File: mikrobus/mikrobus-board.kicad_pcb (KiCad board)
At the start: 2 copper layers, 66 x 63.5 mm, 9 parts, among them J1 Conn_01x06, P3 microBus_1, P4 microBus_2, P5 microBus_1, P6 microBus_2

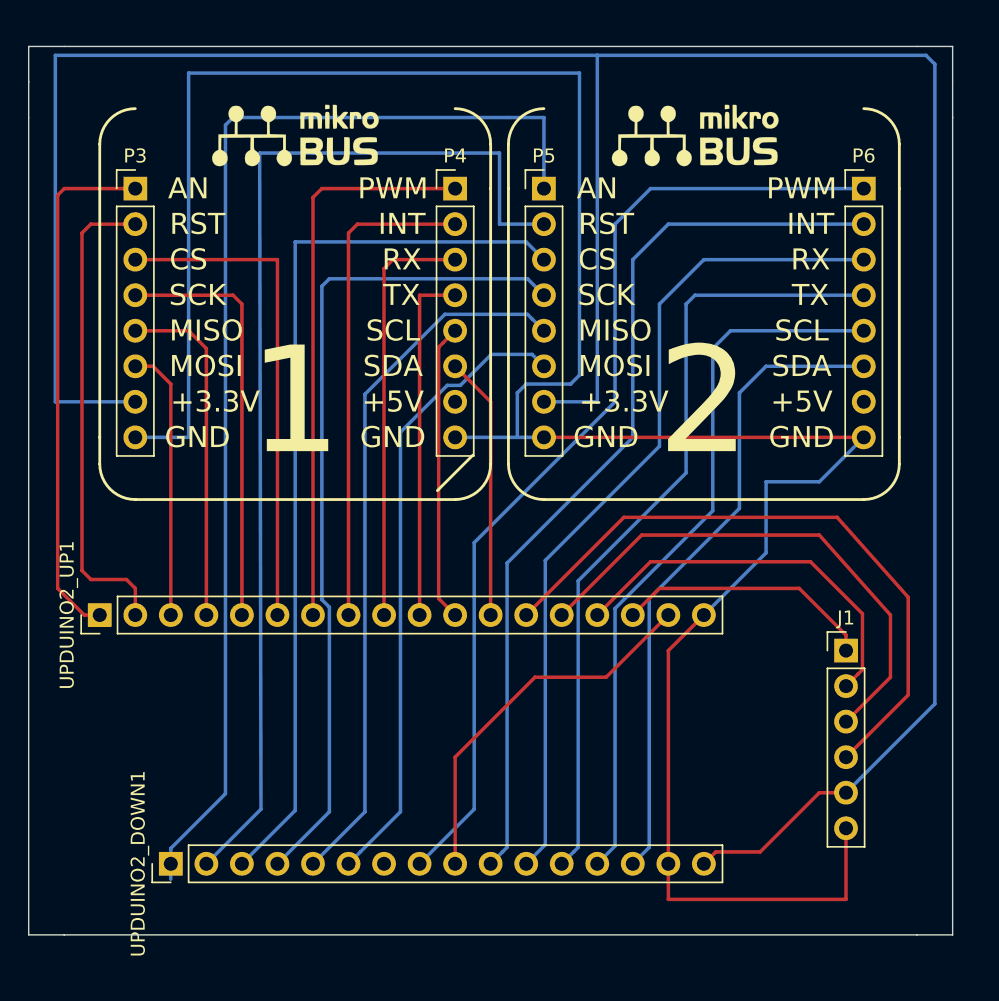
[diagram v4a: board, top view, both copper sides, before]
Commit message: Power lines and better routing for power lines
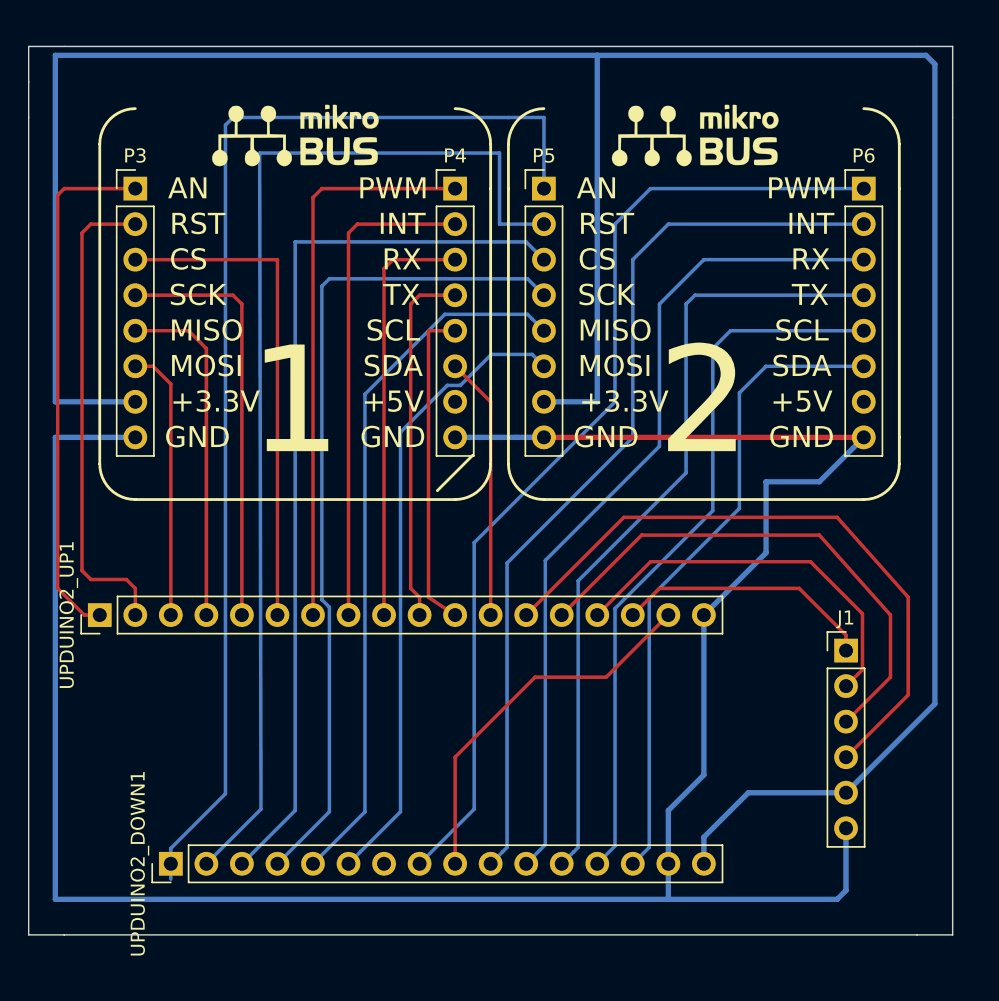
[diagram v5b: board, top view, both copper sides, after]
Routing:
- net GND: track 175.5 -> 170.2 mm
- net /SCL_1: track 21.3 -> 23.2 mm
- net +3V3: track 189.1 -> 190.3 mm
- net /TX_1: track 25.4 -> 25.9 mm
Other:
- net class Power added: clearance 0.25, trace_width 0.38, via_dia 0.4, via_drill 0.3
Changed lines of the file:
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@@
     (links 38)
     (no_connects 0)
-    (area 116.789999 101.549999 182.930001 165.150001)
+    (area 116.789999 101.549999 182.930001 167.005714)
     (thickness 1.6)
     (drawings 69)
-    (tracks 177)
+    (tracks 176)
     (zones 0)
     (modules 9)
@@
       (outputformat 1)
       (mirror false)
-      (drillshape 1)
+      (drillshape 0)
       (scaleselection 1)
       (outputdirectory ""))
@@
     (uvia_dia 0.3)
     (uvia_drill 0.1)
-    (add_net +3V3)
     (add_net /AN_1)
     (add_net /AN_2)
@@
     (add_net /TX_1)
     (add_net /TX_2)
-    (add_net GND)
     (add_net "Net-(P4-Pad7)")
     (add_net "Net-(P6-Pad7)")
     (add_net "Net-(UPDUINO2_DOWN1-Pad7)")
+  )
+  (net_class Power ""
+    (clearance 0.25)
+    (trace_width 0.38)
+    (via_dia 0.4)
+    (via_drill 0.3)
+    (uvia_dia 0.3)
+    (uvia_drill 0.1)
+    (add_net +3V3)
+    (add_net GND)
   )
   (module Graphics:mikrobus (layer F.Cu)
@@
   (segment (start 127 125.73) (end 127 142.24) (width 0.25) (layer F.Cu) (net 10))
   (segment (start 125.73 124.46) (end 127 125.73) (width 0.25) (layer F.Cu) (net 10))
-  (segment (start 118.745 102.235) (end 157.48 102.235) (width 0.25) (layer B.Cu) (net 11))
-  (segment (start 153.67 127) (end 157.48 127) (width 0.25) (layer B.Cu) (net 11))
-  (segment (start 157.48 102.235) (end 180.975 102.235) (width 0.25) (layer B.Cu) (net 11))
-  (segment (start 157.48 127) (end 157.48 102.235) (width 0.25) (layer B.Cu) (net 11))
-  (segment (start 181.61 148.59) (end 175.26 154.94) (width 0.25) (layer B.Cu) (net 11))
-  (segment (start 181.61 102.87) (end 181.61 148.59) (width 0.25) (layer B.Cu) (net 11))
-  (segment (start 180.975 102.235) (end 181.61 102.87) (width 0.25) (layer B.Cu) (net 11))
-  (segment (start 118.745 127) (end 118.745 102.235) (width 0.25) (layer B.Cu) (net 11))
-  (segment (start 124.46 127) (end 118.745 127) (width 0.25) (layer B.Cu) (net 11))
-  (segment (start 169.124999 159.170001) (end 173.355 154.94) (width 0.25) (layer F.Cu) (net 11))
-  (segment (start 173.355 154.94) (end 175.26 154.94) (width 0.25) (layer F.Cu) (net 11))
-  (segment (start 165.1 160.02) (end 165.949999 159.170001) (width 0.25) (layer F.Cu) (net 11))
-  (segment (start 165.949999 159.170001) (end 169.124999 159.170001) (width 0.25) (layer F.Cu) (net 11))
-  (segment (start 124.46 129.54) (end 128.27 129.54) (width 0.25) (layer B.Cu) (net 12))
-  (segment (start 151.765 126.365) (end 151.765 129.54) (width 0.25) (layer B.Cu) (net 12))
-  (segment (start 152.4 125.73) (end 151.765 126.365) (width 0.25) (layer B.Cu) (net 12))
-  (segment (start 155.575 125.73) (end 152.4 125.73) (width 0.25) (layer B.Cu) (net 12))
-  (segment (start 156.21 125.095) (end 155.575 125.73) (width 0.25) (layer B.Cu) (net 12))
-  (segment (start 156.21 103.505) (end 156.21 125.095) (width 0.25) (layer B.Cu) (net 12))
-  (segment (start 128.27 103.505) (end 156.21 103.505) (width 0.25) (layer B.Cu) (net 12))
-  (segment (start 128.27 129.54) (end 128.27 103.505) (width 0.25) (layer B.Cu) (net 12))
-  (segment (start 153.67 129.54) (end 152.467919 129.54) (width 0.25) (layer B.Cu) (net 12))
-  (segment (start 152.467919 129.54) (end 151.765 129.54) (width 0.25) (layer B.Cu) (net 12))
-  (segment (start 151.765 129.54) (end 147.32 129.54) (width 0.25) (layer B.Cu) (net 12))
-  (segment (start 176.53 129.54) (end 153.67 129.54) (width 0.25) (layer F.Cu) (net 12))
-  (segment (start 169.545 132.715) (end 173.355 132.715) (width 0.25) (layer B.Cu) (net 12))
-  (segment (start 173.355 132.715) (end 176.53 129.54) (width 0.25) (layer B.Cu) (net 12))
-  (segment (start 169.545 137.795) (end 169.545 132.715) (width 0.25) (layer B.Cu) (net 12))
-  (segment (start 165.1 142.24) (end 169.545 137.795) (width 0.25) (layer B.Cu) (net 12))
-  (segment (start 162.56 144.78) (end 165.1 142.24) (width 0.25) (layer F.Cu) (net 12))
-  (segment (start 162.56 160.02) (end 162.56 144.78) (width 0.25) (layer F.Cu) (net 12))
-  (segment (start 175.26 162.56) (end 175.26 157.48) (width 0.25) (layer F.Cu) (net 12))
-  (segment (start 162.56 162.56) (end 175.26 162.56) (width 0.25) (layer F.Cu) (net 12))
-  (segment (start 162.56 160.02) (end 162.56 162.56) (width 0.25) (layer F.Cu) (net 12))
+  (segment (start 165.1 160.02) (end 165.1 158.115) (width 0.38) (layer B.Cu) (net 11) (status 400000))
+  (segment (start 168.275 154.94) (end 175.26 154.94) (width 0.38) (layer B.Cu) (net 11) (status 800000))
+  (segment (start 165.1 158.115) (end 168.275 154.94) (width 0.38) (layer B.Cu) (net 11))
+  (segment (start 118.745 102.235) (end 157.48 102.235) (width 0.38) (layer B.Cu) (net 11))
+  (segment (start 153.67 127) (end 157.48 127) (width 0.38) (layer B.Cu) (net 11))
+  (segment (start 157.48 102.235) (end 180.975 102.235) (width 0.38) (layer B.Cu) (net 11))
+  (segment (start 157.48 127) (end 157.48 102.235) (width 0.38) (layer B.Cu) (net 11))
+  (segment (start 181.61 148.59) (end 175.26 154.94) (width 0.38) (layer B.Cu) (net 11))
+  (segment (start 181.61 102.87) (end 181.61 148.59) (width 0.38) (layer B.Cu) (net 11))
+  (segment (start 180.975 102.235) (end 181.61 102.87) (width 0.38) (layer B.Cu) (net 11))
+  (segment (start 118.745 127) (end 118.745 102.235) (width 0.38) (layer B.Cu) (net 11))
+  (segment (start 124.46 127) (end 118.745 127) (width 0.38) (layer B.Cu) (net 11))
+  (segment (start 165.1 142.24) (end 165.1 153.67) (width 0.38) (layer B.Cu) (net 12) (status 400000))
+  (segment (start 162.56 156.21) (end 162.56 160.02) (width 0.38) (layer B.Cu) (net 12) (status 800000))
+  (segment (start 165.1 153.67) (end 162.56 156.21) (width 0.38) (layer B.Cu) (net 12))
+  (segment (start 175.26 157.48) (end 175.26 161.925) (width 0.38) (layer B.Cu) (net 12) (status 400000))
+  (segment (start 174.625 162.56) (end 162.56 162.56) (width 0.38) (layer B.Cu) (net 12))
+  (segment (start 175.26 161.925) (end 174.625 162.56) (width 0.38) (layer B.Cu) (net 12))
+  (segment (start 124.46 129.54) (end 118.745 129.54) (width 0.38) (layer B.Cu) (net 12))
+  (segment (start 162.56 162.56) (end 162.56 160.02) (width 0.38) (layer B.Cu) (net 12))
+  (segment (start 118.745 162.56) (end 162.56 162.56) (width 0.38) (layer B.Cu) (net 12))
+  (segment (start 118.745 129.54) (end 118.745 162.56) (width 0.38) (layer B.Cu) (net 12))
+  (segment (start 153.67 129.54) (end 152.467919 129.54) (width 0.38) (layer B.Cu) (net 12))
+  (segment (start 152.467919 129.54) (end 151.765 129.54) (width 0.38) (layer B.Cu) (net 12))
+  (segment (start 151.765 129.54) (end 147.32 129.54) (width 0.38) (layer B.Cu) (net 12))
+  (segment (start 176.53 129.54) (end 153.67 129.54) (width 0.38) (layer F.Cu) (net 12))
+  (segment (start 169.545 132.715) (end 173.355 132.715) (width 0.38) (layer B.Cu) (net 12))
+  (segment (start 173.355 132.715) (end 176.53 129.54) (width 0.38) (layer B.Cu) (net 12))
+  (segment (start 169.545 137.795) (end 169.545 132.715) (width 0.38) (layer B.Cu) (net 12))
+  (segment (start 165.1 142.24) (end 169.545 137.795) (width 0.38) (layer B.Cu) (net 12))
   (segment (start 137.795 111.76) (end 147.32 111.76) (width 0.25) (layer F.Cu) (net 13))
   (segment (start 137.16 112.395) (end 137.795 111.76) (width 0.25) (layer F.Cu) (net 13))
@@
   (segment (start 142.875 116.84) (end 147.32 116.84) (width 0.25) (layer F.Cu) (net 15))
   (segment (start 142.24 142.24) (end 142.24 117.475) (width 0.25) (layer F.Cu) (net 15))
+  (segment (start 144.78 142.24) (end 144.78 140.97) (width 0.25) (layer F.Cu) (net 16))
   (segment (start 144.78 119.38) (end 147.32 119.38) (width 0.25) (layer F.Cu) (net 16))
-  (segment (start 144.78 142.24) (end 144.78 119.38) (width 0.25) (layer F.Cu) (net 16))
-  (segment (start 147.32 142.24) (end 146.144999 141.064999) (width 0.25) (layer F.Cu) (net 17))
-  (segment (start 146.144999 141.064999) (end 146.144999 123.095001) (width 0.25) (layer F.Cu) (net 17))
-  (segment (start 146.470001 122.769999) (end 147.32 121.92) (width 0.25) (layer F.Cu) (net 17))
-  (segment (start 146.144999 123.095001) (end 146.470001 122.769999) (width 0.25) (layer F.Cu) (net 17))
+  (segment (start 144.145 120.015) (end 144.78 119.38) (width 0.25) (layer F.Cu) (net 16))
+  (segment (start 144.145 140.335) (end 144.145 120.015) (width 0.25) (layer F.Cu) (net 16))
+  (segment (start 144.78 140.97) (end 144.145 140.335) (width 0.25) (layer F.Cu) (net 16))
+  (segment (start 147.32 142.24) (end 145.415 140.97) (width 0.25) (layer F.Cu) (net 17))
+  (segment (start 145.415 140.97) (end 145.415 121.92) (width 0.25) (layer F.Cu) (net 17))
+  (segment (start 146.685 121.92) (end 147.32 121.92) (width 0.25) (layer F.Cu) (net 17))
+  (segment (start 145.415 121.92) (end 146.685 121.92) (width 0.25) (layer F.Cu) (net 17))
   (segment (start 149.86 142.24) (end 149.86 127) (width 0.25) (layer F.Cu) (net 18))
   (segment (start 149.86 127) (end 147.32 124.46) (width 0.25) (layer F.Cu) (net 18))

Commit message: Finished design
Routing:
- added copper zone on F.Cu, net +3V3
- added copper zone on B.Cu, net GND
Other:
- board size 66 x 63.5 mm -> 67.3 x 64.8 mm
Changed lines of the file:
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@@
     (links 38)
     (no_connects 0)
-    (area 116.789999 101.549999 182.930001 167.005714)
+    (area 116.789999 100.279999 184.200001 165.150001)
     (thickness 1.6)
-    (drawings 69)
+    (drawings 70)
     (tracks 176)
     (zones 0)
@@
       (xy 2.292195 -2.172368) (xy 2.384376 -2.169505)) (layer F.SilkS) (width 0.01))
   )
+  (gr_line (start 184.15 100.33) (end 184.15 165.1) (angle 90) (layer Edge.Cuts) (width 0.1))
+  (gr_line (start 184.15 165.1) (end 182.88 165.1) (angle 90) (layer Edge.Cuts) (width 0.1))
+  (gr_line (start 182.88 100.33) (end 184.15 100.33) (angle 90) (layer Edge.Cuts) (width 0.1))
+  (gr_line (start 180.34 100.33) (end 182.88 100.33) (angle 90) (layer Edge.Cuts) (width 0.1))
+  (gr_line (start 116.84 100.33) (end 116.84 101.6) (angle 90) (layer Edge.Cuts) (width 0.1))
+  (gr_line (start 119.38 100.33) (end 116.84 100.33) (angle 90) (layer Edge.Cuts) (width 0.1))
   (gr_text 1 (at 135.89 127) (layer F.SilkS)
     (effects (font (size 7.62 7.62) (thickness 0.762)))
   )
   (gr_line (start 116.84 101.6) (end 116.84 104.14) (layer Edge.Cuts) (width 0.1))
-  (gr_line (start 182.88 101.6) (end 182.88 104.14) (layer Edge.Cuts) (width 0.1))
   (gr_text PWM (at 172.085 111.76) (layer F.SilkS)
     (effects (font (size 1.5 1.5) (thickness 0.3)))
@@
   )
   (gr_line (start 180.34 165.1) (end 182.88 165.1) (layer Edge.Cuts) (width 0.1))
-  (gr_line (start 180.34 101.6) (end 182.88 101.6) (layer Edge.Cuts) (width 0.1))
   (gr_text 2 (at 165.1 127) (layer F.SilkS)
     (effects (font (size 7.62 7.62) (thickness 0.762)))
@@
   (gr_line (start 151.13 111.76) (end 151.13 129.54) (layer F.SilkS) (width 0.2))
   (gr_arc (start 153.67 108.585) (end 151.13 108.585) (angle 90) (layer F.SilkS) (width 0.2))
-  (gr_line (start 182.88 104.14) (end 182.88 106.68) (layer Edge.Cuts) (width 0.1))
   (gr_line (start 116.84 106.68) (end 116.84 104.14) (layer Edge.Cuts) (width 0.1))
   (gr_line (start 148.59 130.81) (end 146.05 133.35) (layer F.SilkS) (width 0.2))
@@
   (gr_line (start 116.84 165.1) (end 119.38 165.1) (layer Edge.Cuts) (width 0.1))
   (gr_line (start 116.84 106.68) (end 116.84 165.1) (layer Edge.Cuts) (width 0.1))
-  (gr_line (start 119.38 101.6) (end 116.84 101.6) (layer Edge.Cuts) (width 0.1))
   (gr_line (start 180.34 165.1) (end 119.38 165.1) (layer Edge.Cuts) (width 0.1))
-  (gr_line (start 182.88 106.68) (end 182.88 165.1) (layer Edge.Cuts) (width 0.1))
-  (gr_line (start 119.38 101.6) (end 180.34 101.6) (layer Edge.Cuts) (width 0.1))
+  (gr_line (start 119.38 100.33) (end 180.34 100.33) (layer Edge.Cuts) (width 0.1))
   (segment (start 152.4 142.24) (end 159.385 135.255) (width 0.25) (layer F.Cu) (net 1))
   (segment (start 179.705 147.955) (end 179.705 147.955) (width 0.25) (layer F.Cu) (net 1))
@@
   (segment (start 127 125.73) (end 127 142.24) (width 0.25) (layer F.Cu) (net 10))
   (segment (start 125.73 124.46) (end 127 125.73) (width 0.25) (layer F.Cu) (net 10))
-  (segment (start 165.1 160.02) (end 165.1 158.115) (width 0.38) (layer B.Cu) (net 11) (status 400000))
-  (segment (start 168.275 154.94) (end 175.26 154.94) (width 0.38) (layer B.Cu) (net 11) (status 800000))
+  (segment (start 165.1 160.02) (end 165.1 158.115) (width 0.38) (layer B.Cu) (net 11))
+  (segment (start 168.275 154.94) (end 175.26 154.94) (width 0.38) (layer B.Cu) (net 11))
   (segment (start 165.1 158.115) (end 168.275 154.94) (width 0.38) (layer B.Cu) (net 11))
   (segment (start 118.745 102.235) (end 157.48 102.235) (width 0.38) (layer B.Cu) (net 11))
@@
   (segment (start 118.745 127) (end 118.745 102.235) (width 0.38) (layer B.Cu) (net 11))
   (segment (start 124.46 127) (end 118.745 127) (width 0.38) (layer B.Cu) (net 11))
-  (segment (start 165.1 142.24) (end 165.1 153.67) (width 0.38) (layer B.Cu) (net 12) (status 400000))
-  (segment (start 162.56 156.21) (end 162.56 160.02) (width 0.38) (layer B.Cu) (net 12) (status 800000))
+  (segment (start 165.1 142.24) (end 165.1 153.67) (width 0.38) (layer B.Cu) (net 12))
+  (segment (start 162.56 156.21) (end 162.56 160.02) (width 0.38) (layer B.Cu) (net 12))
   (segment (start 165.1 153.67) (end 162.56 156.21) (width 0.38) (layer B.Cu) (net 12))
-  (segment (start 175.26 157.48) (end 175.26 161.925) (width 0.38) (layer B.Cu) (net 12) (status 400000))
+  (segment (start 175.26 157.48) (end 175.26 161.925) (width 0.38) (layer B.Cu) (net 12))
   (segment (start 174.625 162.56) (end 162.56 162.56) (width 0.38) (layer B.Cu) (net 12))
   (segment (start 175.26 161.925) (end 174.625 162.56) (width 0.38) (layer B.Cu) (net 12))
@@
   (segment (start 158.115 146.685) (end 153.035 146.685) (width 0.25) (layer F.Cu) (net 34))
   (segment (start 162.56 142.24) (end 158.115 146.685) (width 0.25) (layer F.Cu) (net 34))
+  (zone (net 11) (net_name +3V3) (layer F.Cu) (hatch edge 0.508)
+    (connect_pads (clearance 0.508))
+    (min_thickness 0.254)
+    (fill yes (arc_segments 16) (thermal_gap 0.508) (thermal_bridge_width 0.508))
+    (polygon
+      (pts
+        (xy 182.88 163.83) (xy 118.11 163.83) (xy 118.11 101.6) (xy 182.88 101.6)
+      )
+    )
+  )
+  (zone (net 12) (net_name GND) (layer B.Cu) (hatch edge 0.508)
+    (connect_pads (clearance 0.508))
+    (min_thickness 0.254)
+    (fill yes (arc_segments 16) (thermal_gap 0.508) (thermal_bridge_width 0.508))
+    (polygon
+      (pts
+        (xy 182.88 163.83) (xy 118.11 163.83) (xy 118.11 101.6) (xy 182.88 101.6)
+      )
+    )
+  )
 )
